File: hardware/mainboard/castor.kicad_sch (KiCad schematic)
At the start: 46 parts, among them J7 OSC OUT, Q1 MMBT3906, U10 MCP6001-OT, U7 TL074, U8 TL074, U9 74LVC2G74

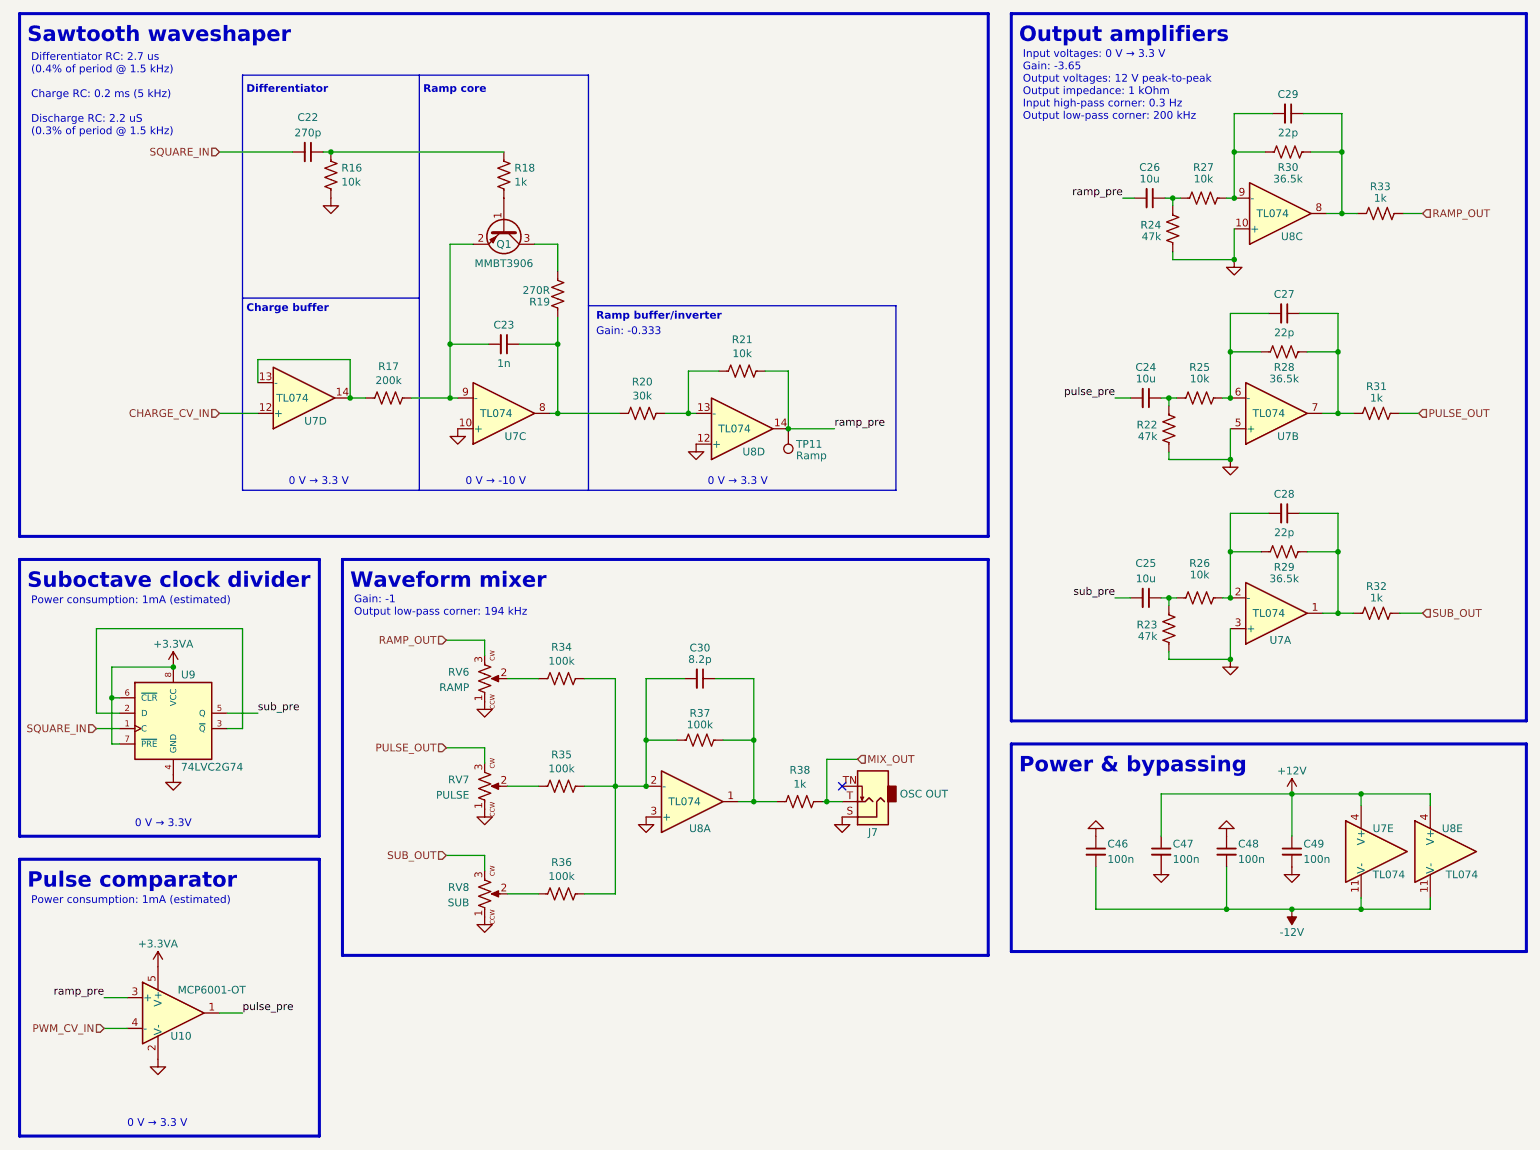
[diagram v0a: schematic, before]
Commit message: Audit BOM, replace some parts with alts
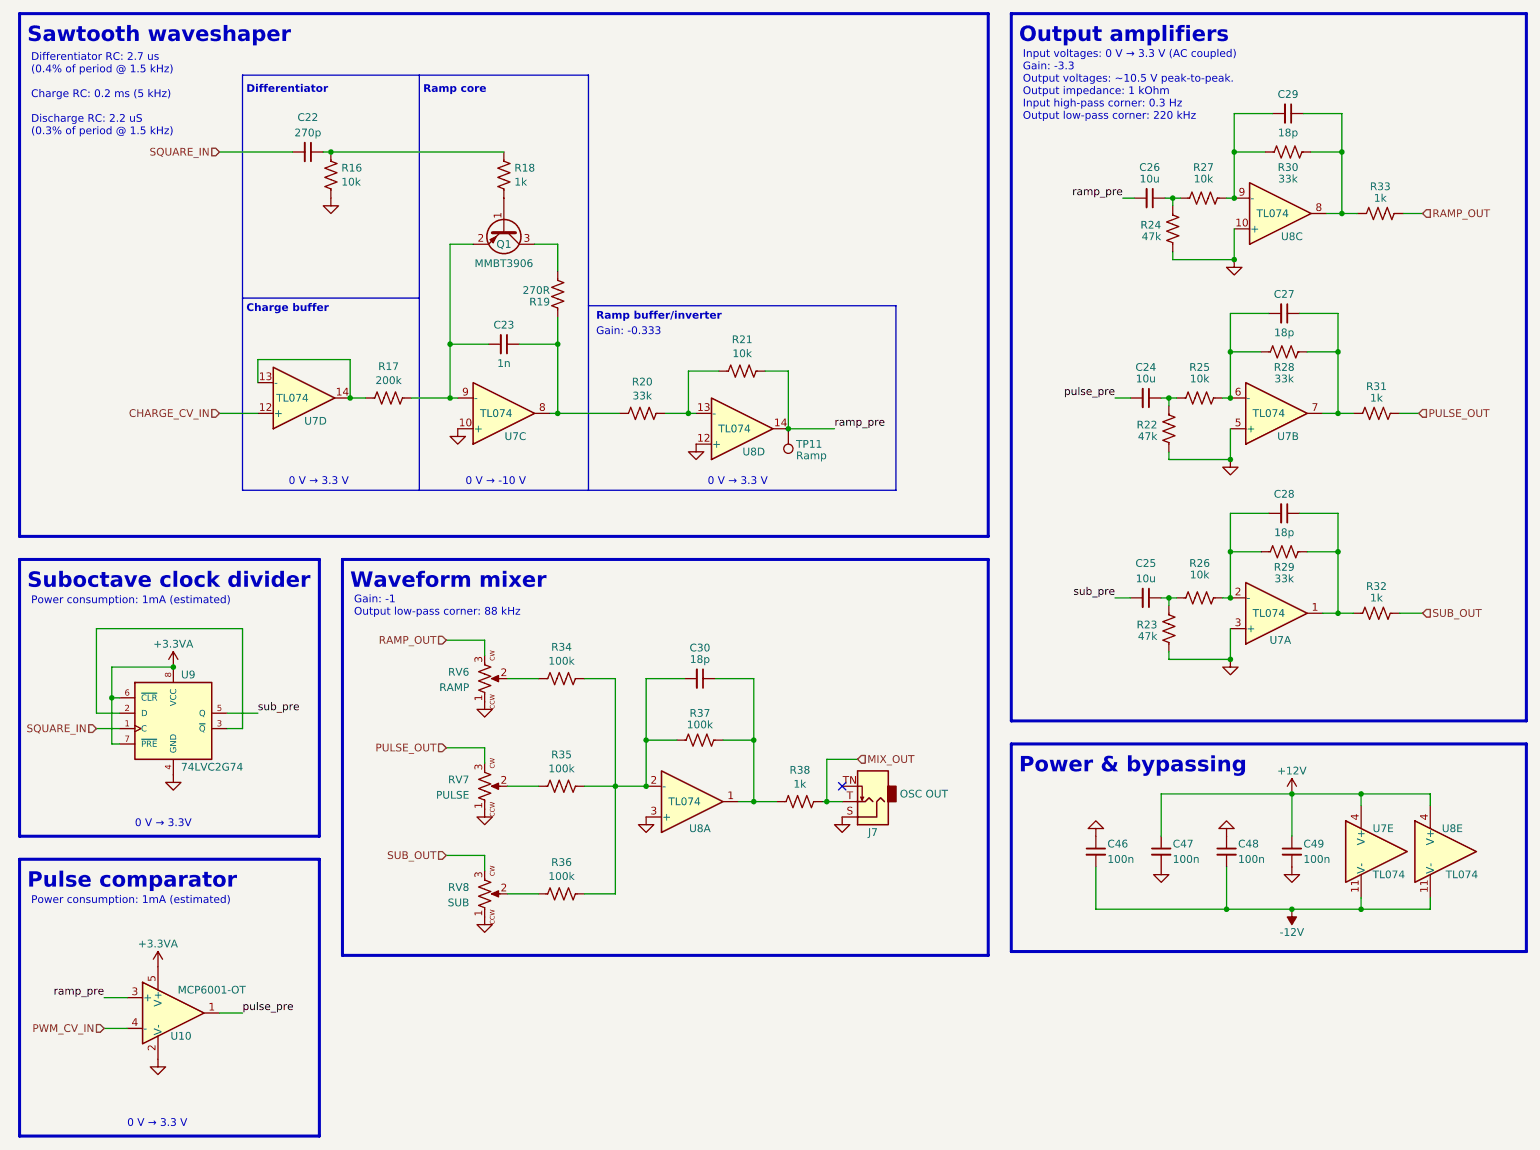
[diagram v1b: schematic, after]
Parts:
- C22: finalized (none) -> yes; mpn (none) -> GCM1555C1H271FA16D
- C23: Reqs Ramp core, C0G 1% or better, 6 V -> Ramp core, C0G 1% or better, 25 V; finalized (none) -> yes; mpn (none) -> GCM1555C1H102FA16D, GRM1555C1H102FA01D
- C24, C25, C26, U10, U7, U8, U9: finalized (none) -> yes
- C27, C28, C29: value 22p -> 18p; finalized (none) -> yes; mpn (none) -> CL05C180JB5NNNC
- C30: value 8.2p -> 18p; finalized (none) -> yes; mpn (none) -> CL05C180JB5NNNC
- C46, C47, C48, C49: finalized (none) -> yes; macrofab_mpn (none) -> MF-CAP-0402-0.1uF; mpn (none) -> CL05B104KO5NNNC
- R16: Reqs Digital control path, 1%, 15 mW -> Digital control path, 1%, 100 mW, thin film
- R17: Reqs Analog control path, 0.5%, 1 mW -> Analog control path, 0.5%, 100 mW, thin film
- R18: Reqs Digital control path, 5%, 12 mW -> Digital control path, 5%, 100 mW, thin film
- R19: Reqs Ramp core, 1%, 50 mW -> Ramp core, 1%, 100 mW, thin film
- R20: value 30k -> 33k; Reqs Low voltage audio, 1%, 5 mW -> Low voltage audio, 1%, 100 mW, thin film
- R21, R25, R26, R27: Reqs Low voltage audio, 1%, 15 mW -> Low voltage audio, 1%, 100 mW, thin film
- R22, R23, R24: Reqs Low voltage audio, 1%, 15 mW -> Low voltage audio, 1%, 100, thin film
- R28, R29, R30: value 36.5k -> 33k; Reqs Eurorack level audio, 1%, 5 mW -> Eurorack level audio, 1%, 100 mW, thin film
- R31, R32, R33, R38: Reqs Output impedance, 5%, 150 mW -> Output impedance, 5%, 150 mW, thin film
- R34, R35, R36, R37: Reqs Eurorack level audio, 1%, 2 mW -> Eurorack level audio, 1%, 100 mW, thin film
- RV6, RV7, RV8: Reqs (none) -> 10k, linear or audio taper, 9mm tall trimmer pot with white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; finalized (none) -> yes; mpn R0904N-???? L-25KQ/LWS -> R0904N-B10K L-25KQ/LWS
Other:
- note added: "Gain: -1 Output low-pass corner: 88 kHz"
- note added: "Input voltages: 0 V → 3.3 V (AC coupled) Gain: -3.3 Output voltages: ~10.5 V peak-to-peak. Output impedance: 1 kOhm Input high-pass corner: 0.3 Hz Output low-pass corner: 220 kHz"
- note removed: "Gain: -1 Output low-pass corner: 194 kHz"
- note removed: "Input voltages: 0 V → 3.3 V Gain: -3.65 Output voltages: 12 V peak-to-peak Output impedance: 1 kOhm Input high-pass corner: 0.3 Hz Output low-pass corner: 200 kHz"

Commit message: A little more schematic cleanup
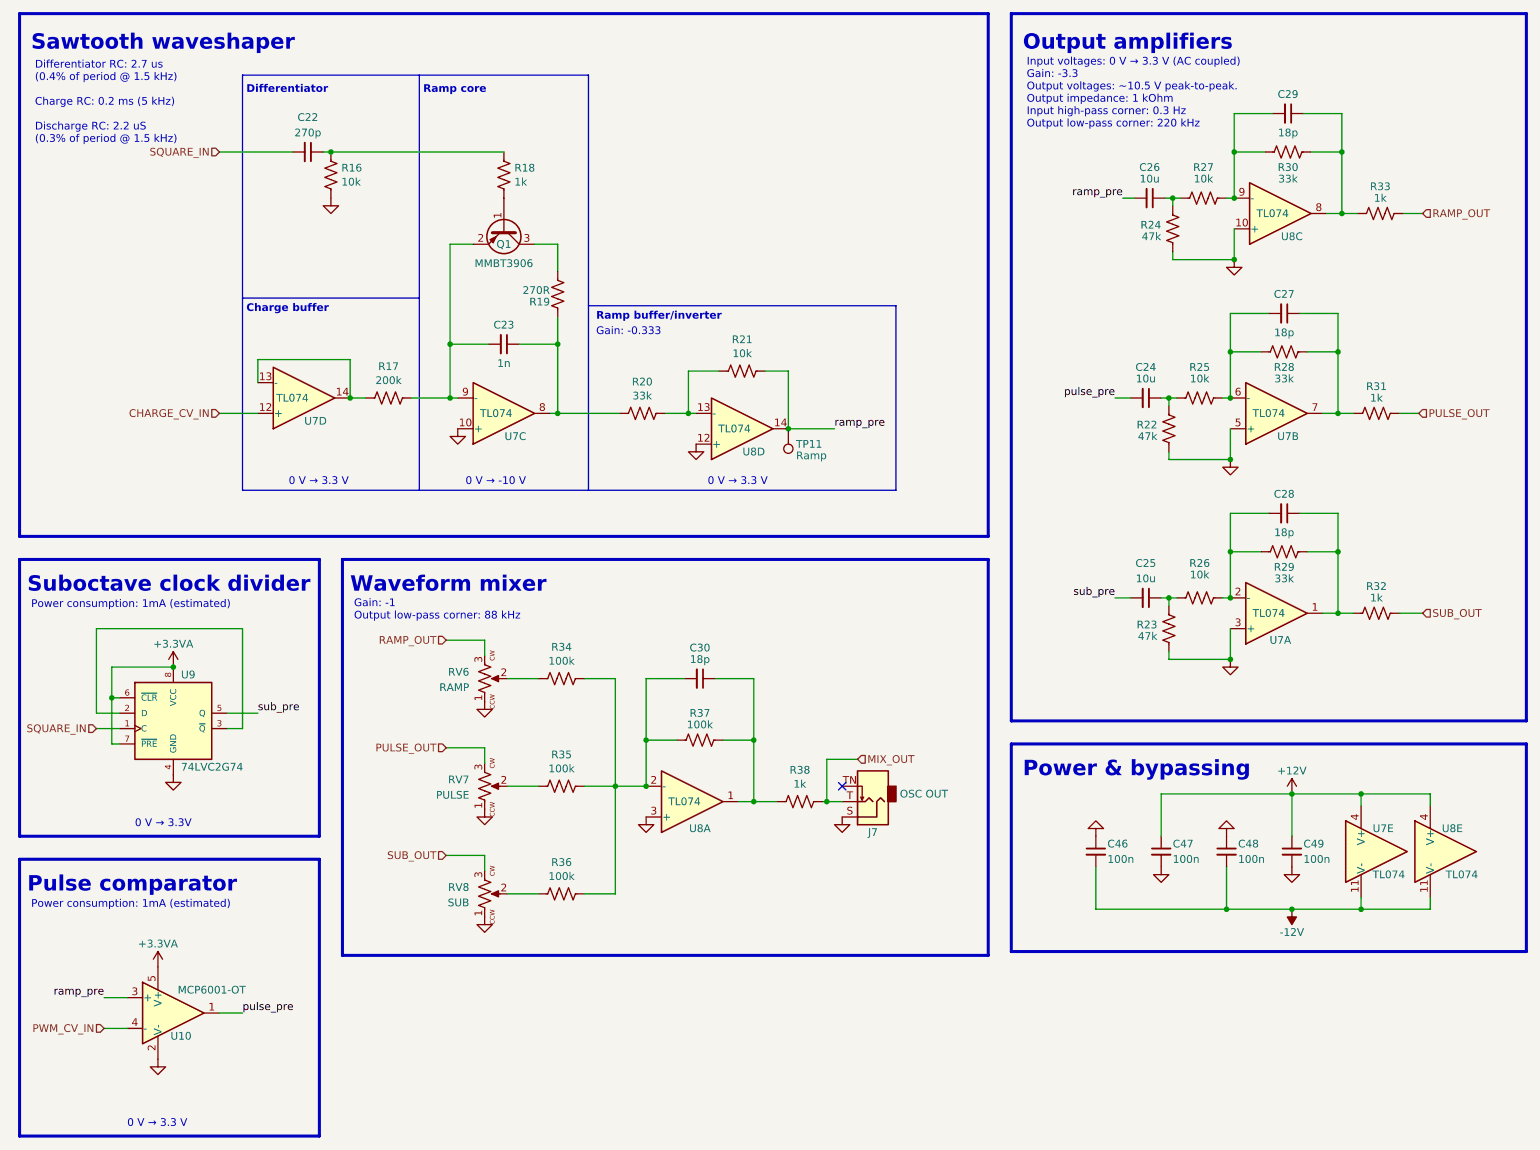
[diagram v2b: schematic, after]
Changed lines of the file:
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@@
     (effects (font (size 1.27 1.27) (thickness 0.254) bold) (justify left bottom))
   )
-  (text "Suboctave clock divider" (at 16.51 110.49 0)
+  (text "Suboctave clock divider" (at 16.51 111.125 0)
     (effects (font (size 2.54 2.54) bold) (justify left bottom))
   )
-  (text "Power & bypassing" (at 180.34 140.97 0)
+  (text "Power & bypassing" (at 180.975 141.605 0)
     (effects (font (size 2.54 2.54) bold) (justify left bottom))
   )
-  (text "Output amplifiers" (at 180.34 20.32 0)
+  (text "Output amplifiers" (at 180.975 21.59 0)
     (effects (font (size 2.54 2.54) (thickness 0.508) bold) (justify left bottom))
   )
@@
     (effects (font (size 1.27 1.27)) (justify left bottom))
   )
-  (text "Gain: -1\nOutput low-pass corner: 88 kHz" (at 70.485 114.935 0)
+  (text "Gain: -1\nOutput low-pass corner: 88 kHz" (at 70.485 115.57 0)
     (effects (font (size 1.27 1.27)) (justify left bottom))
   )
@@
     (effects (font (size 1.27 1.27) (thickness 0.254) bold) (justify left bottom))
   )
-  (text "Sawtooth waveshaper" (at 16.51 20.32 0)
+  (text "Sawtooth waveshaper" (at 17.145 21.59 0)
     (effects (font (size 2.54 2.54) (thickness 0.508) bold) (justify left bottom))
   )
-  (text "Power consumption: 1mA (estimated)" (at 17.145 113.03 0)
+  (text "Power consumption: 1mA (estimated)" (at 17.145 113.665 0)
     (effects (font (size 1.27 1.27)) (justify left bottom))
   )
-  (text "Power consumption: 1mA (estimated)" (at 17.145 162.56 0)
+  (text "Power consumption: 1mA (estimated)" (at 17.145 163.195 0)
     (effects (font (size 1.27 1.27)) (justify left bottom))
   )
@@
     (effects (font (size 1.27 1.27)) (justify left bottom))
   )
-  (text "Waveform mixer" (at 69.85 110.49 0)
+  (text "Waveform mixer" (at 69.85 111.125 0)
     (effects (font (size 2.54 2.54) bold) (justify left bottom))
   )
@@
     (effects (font (size 1.27 1.27)) (justify left bottom))
   )
-  (text "Pulse comparator" (at 16.51 160.02 0)
+  (text "Pulse comparator" (at 16.51 160.655 0)
     (effects (font (size 2.54 2.54) bold) (justify left bottom))
   )
   (text "Differentiator RC: 2.7 us\n(0.4% of period @ 1.5 kHz)\n\nCharge RC: 0.2 ms (5 kHz)\n\nDischarge RC: 2.2 uS\n(0.3% of period @ 1.5 kHz)"
-    (at 17.145 35.56 0)
+    (at 17.78 36.83 0)
     (effects (font (size 1.27 1.27)) (justify left bottom))
   )
@@
   )
   (text "Input voltages: 0 V → 3.3 V (AC coupled)\nGain: -3.3\nOutput voltages: ~10.5 V peak-to-peak.\nOutput impedance: 1 kOhm\nInput high-pass corner: 0.3 Hz\nOutput low-pass corner: 220 kHz"
-    (at 180.975 33.02 0)
+    (at 181.61 34.29 0)
     (effects (font (size 1.27 1.27)) (justify left bottom))
   )

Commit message: Finalize resistor mpns
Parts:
- R16, R21, R25, R26, R27: mpn (none) -> RR0510P-103-D
- R17: mpn (none) -> RC0402FR-07200KL
- R18: mpn (none) -> RC0402JR-071KL
- R19: mpn (none) -> CRGCQ0402F270R
- R20, R28, R29, R30: mpn (none) -> RC0402FR-0733KL
- R22, R23, R24: mpn (none) -> RC0402FR-0747KL
- R34, R35, R36, R37: mpn (none) -> RC0402DR-07100KL
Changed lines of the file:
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@@
       (effects (font (size 1.27 1.27)) hide)
     )
-    (property "mpn" "" (id 5) (at 95.25 41.91 0)
+    (property "mpn" "RC0402JR-071KL" (id 5) (at 95.25 41.91 0)
       (effects (font (size 1.27 1.27)) hide)
     )
@@
       (effects (font (size 1.27 1.27)) hide)
     )
-    (property "mpn" "" (id 5) (at 66.675 41.91 0)
+    (property "mpn" "RR0510P-103-D" (id 5) (at 66.675 41.91 0)
       (effects (font (size 1.27 1.27)) hide)
     )
@@
       (effects (font (size 1.27 1.27)) hide)
     )
-    (property "mpn" "" (id 5) (at 76.2 78.74 0)
+    (property "mpn" "RC0402FR-07200KL" (id 5) (at 76.2 78.74 0)
       (effects (font (size 1.27 1.27)) hide)
     )
@@
       (effects (font (size 1.27 1.27)) hide)
     )
-    (property "mpn" "" (id 5) (at 118.11 81.28 0)
+    (property "mpn" "RC0402FR-0733KL" (id 5) (at 118.11 81.28 0)
       (effects (font (size 1.27 1.27)) hide)
     )
@@
       (effects (font (size 1.27 1.27)) hide)
     )
-    (property "mpn" "" (id 5) (at 134.62 74.295 0)
+    (property "mpn" "RR0510P-103-D" (id 5) (at 134.62 74.295 0)
       (effects (font (size 1.27 1.27)) hide)
     )
@@
       (effects (font (size 1.27 1.27)) hide)
     )
-    (property "mpn" "" (id 5) (at 210.82 45.72 0)
+    (property "mpn" "RR0510P-103-D" (id 5) (at 210.82 45.72 0)
       (effects (font (size 1.27 1.27)) hide)
     )
@@
       (effects (font (size 1.27 1.27)) hide)
     )
-    (property "mpn" "" (id 5) (at 224.79 38.1 0)
+    (property "mpn" "RC0402FR-0733KL" (id 5) (at 224.79 38.1 0)
       (effects (font (size 1.27 1.27)) hide)
     )
@@
       (effects (font (size 1.27 1.27)) hide)
     )
-    (property "mpn" "" (id 5) (at 127.635 135.255 0)
+    (property "mpn" "RC0402DR-07100KL" (id 5) (at 127.635 135.255 0)
       (effects (font (size 1.27 1.27)) hide)
     )
@@
       (effects (font (size 1.27 1.27)) hide)
     )
-    (property "mpn" "" (id 5) (at 104.775 125.095 0)
+    (property "mpn" "RC0402DR-07100KL" (id 5) (at 104.775 125.095 0)
       (effects (font (size 1.27 1.27)) hide)
     )
@@
       (effects (font (size 1.27 1.27)) hide)
     )
-    (property "mpn" "" (id 5) (at 104.775 142.875 0)
+    (property "mpn" "RC0402DR-07100KL" (id 5) (at 104.775 142.875 0)
       (effects (font (size 1.27 1.27)) hide)
     )
@@
       (effects (font (size 1.27 1.27)) hide)
     )
-    (property "mpn" "" (id 5) (at 104.775 160.655 0)
+    (property "mpn" "RC0402DR-07100KL" (id 5) (at 104.775 160.655 0)
       (effects (font (size 1.27 1.27)) hide)
     )
@@
       (effects (font (size 1.27 1.27)) hide)
     )
-    (property "mpn" "" (id 5) (at 205.74 50.8 0)
+    (property "mpn" "RC0402FR-0747KL" (id 5) (at 205.74 50.8 0)
       (effects (font (size 1.27 1.27)) hide)
     )
@@
       (effects (font (size 1.27 1.27)) hide)
     )
-    (property "mpn" "" (id 5) (at 210.185 78.74 0)
+    (property "mpn" "RR0510P-103-D" (id 5) (at 210.185 78.74 0)
       (effects (font (size 1.27 1.27)) hide)
     )
@@
       (effects (font (size 1.27 1.27)) hide)
     )
-    (property "mpn" "" (id 5) (at 224.155 71.12 0)
+    (property "mpn" "RC0402FR-0733KL" (id 5) (at 224.155 71.12 0)
       (effects (font (size 1.27 1.27)) hide)
     )
@@
       (effects (font (size 1.27 1.27)) hide)
     )
-    (property "mpn" "" (id 5) (at 205.105 83.82 0)
+    (property "mpn" "RC0402FR-0747KL" (id 5) (at 205.105 83.82 0)
       (effects (font (size 1.27 1.27)) hide)
     )
@@
       (effects (font (size 1.27 1.27)) hide)
     )
-    (property "mpn" "" (id 5) (at 210.185 111.76 0)
+    (property "mpn" "RR0510P-103-D" (id 5) (at 210.185 111.76 0)
       (effects (font (size 1.27 1.27)) hide)
     )
@@
       (effects (font (size 1.27 1.27)) hide)
     )
-    (property "mpn" "" (id 5) (at 224.155 104.14 0)
+    (property "mpn" "RC0402FR-0733KL" (id 5) (at 224.155 104.14 0)
       (effects (font (size 1.27 1.27)) hide)
     )
@@
       (effects (font (size 1.27 1.27)) hide)
     )
-    (property "mpn" "" (id 5) (at 205.105 116.84 0)
+    (property "mpn" "RC0402FR-0747KL" (id 5) (at 205.105 116.84 0)
       (effects (font (size 1.27 1.27)) hide)
     )
@@
       (effects (font (size 1.27 1.27)) hide)
     )
-    (property "mpn" "" (id 5) (at 104.14 61.595 0)
-      (effects (font (size 1.27 1.27)) hide)
-    )
+    (property "mpn" "CRGCQ0402F270R" (id 5) (at 104.14 61.595 0)
+      (effects (font (size 1.27 1.27)) hide)
+    )
